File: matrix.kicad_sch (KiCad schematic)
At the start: 136 parts

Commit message: added some submodules
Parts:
- D1, D10, D11, D12, D13, D14, D15, D16, D17, D18, D19, D2, D20, D21, D22, D23, D24, D25, D26, D27, D28, D29, D3, D30, D31, D32, D33, D34, D35, D36, D37, D38, D39, D4, D40, D41, D42, D43, D44, D45, D46, D47, D48, D49, D5, D50, D51, D52, D53, D54, D55, D56, D57, D58, D59, D6, D60, D61, D62, D63, D64, D65, D66, D67, D68, D7, D8, D9: renamed from D?; footprint (none) -> Diode_SMD:D_SOD-123
- SW10: renamed from SW?; value MX_LED -> #8
- SW11: renamed from SW?; value MX_LED -> #9
- SW12: renamed from SW?; value MX_LED -> #0
- SW13: renamed from SW?; value MX_LED -> -_
- SW14: renamed from SW?; value MX_LED -> =+
- SW15: renamed from SW?; value MX_LED -> BKSP
- SW16: renamed from SW?; value MX_LED -> DEL
- SW17: renamed from SW?; value MX_LED -> TAB
- SW18: renamed from SW?; value MX_LED -> Q
- SW19: renamed from SW?; value MX_LED -> W
- SW2: renamed from SW?; value MX_LED -> Esc
- SW20: renamed from SW?; value MX_LED -> E
- SW21: renamed from SW?; value MX_LED -> R
- SW22: renamed from SW?; value MX_LED -> T
- SW23: renamed from SW?; value MX_LED -> Y
- SW24: renamed from SW?; value MX_LED -> U
- SW25: renamed from SW?; value MX_LED -> I
- SW26: renamed from SW?; value MX_LED -> O
- SW27: renamed from SW?; value MX_LED -> P
- SW28: renamed from SW?; value MX_LED -> [{
- SW29: renamed from SW?; value MX_LED -> ]}
- SW3: renamed from SW?; value MX_LED -> #1
- SW30: renamed from SW?; value MX_LED -> \|
- SW31: renamed from SW?; value MX_LED -> HOME
- SW32: renamed from SW?; value MX_LED -> CPLK
- SW33: renamed from SW?; value MX_LED -> A
- SW34: renamed from SW?; value MX_LED -> S
- SW35: renamed from SW?; value MX_LED -> D
- SW36: renamed from SW?; value MX_LED -> F
- SW37: renamed from SW?; value MX_LED -> G
- SW38: renamed from SW?; value MX_LED -> H
- SW39: renamed from SW?; value MX_LED -> J
- SW4: renamed from SW?; value MX_LED -> #2
- SW40: renamed from SW?; value MX_LED -> K
- SW41: renamed from SW?; value MX_LED -> L
- SW42: renamed from SW?; value MX_LED -> ;:
- SW43: renamed from SW?; value MX_LED -> '"
- SW44: renamed from SW?; value MX_LED -> ENTER
- SW45: renamed from SW?; value MX_LED -> PGUP
- SW46: renamed from SW?; value MX_LED -> LSHFT
- SW47: renamed from SW?; value MX_LED -> Z
- SW48: renamed from SW?; value MX_LED -> X
- SW49: renamed from SW?; value MX_LED -> C
- SW5: renamed from SW?; value MX_LED -> #3
- SW50: renamed from SW?; value MX_LED -> V
- SW51: renamed from SW?; value MX_LED -> B
- SW52: renamed from SW?; value MX_LED -> N
- SW53: renamed from SW?; value MX_LED -> M
- SW54: renamed from SW?; value MX_LED -> ,<
- SW55: renamed from SW?; value MX_LED -> .>
- SW56: renamed from SW?; value MX_LED -> /?
- SW57: renamed from SW?; value MX_LED -> RSHFT
- SW58: renamed from SW?; value MX_LED -> UP
- SW59: renamed from SW?; value MX_LED -> PGDN
- SW6: renamed from SW?; value MX_LED -> #4
- SW60: renamed from SW?; value MX_LED -> CTRL
- SW61: renamed from SW?; value MX_LED -> WIN
- SW62: renamed from SW?; value MX_LED -> LALT
- SW63: renamed from SW?; value MX_LED -> SPACE
- SW64: renamed from SW?; value MX_LED -> RALT
- SW65: renamed from SW?; value MX_LED -> FN
- SW66: renamed from SW?; value MX_LED -> FN2
- SW67: renamed from SW?; value MX_LED -> LEFT
- SW68: renamed from SW?; value MX_LED -> DOWN
- SW69: renamed from SW?; value MX_LED -> RIGHT
- SW7: renamed from SW?; value MX_LED -> #5
- SW8: renamed from SW?; value MX_LED -> #6
- SW9: renamed from SW?; value MX_LED -> #7

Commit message: half wiring done
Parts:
- D1: value D_Small -> ESC
- D10: value D_Small -> #9
- D11: value D_Small -> #0
- D12: value D_Small -> -_
- D13: value D_Small -> =+
- D14: value D_Small -> BKSP
- D15: value D_Small -> DEL
- D16: value D_Small -> TAB
- D17: value D_Small -> Q
- D18: value D_Small -> W
- D19: value D_Small -> E
- D2: value D_Small -> #1
- D20: value D_Small -> R
- D21: value D_Small -> T
- D22: value D_Small -> Y
- D23: value D_Small -> U
- D24: value D_Small -> I
- D25: value D_Small -> O
- D26: value D_Small -> P
- D27: value D_Small -> [{
- D28: value D_Small -> ]}
- D29: value D_Small -> \|
- D3: value D_Small -> #2
- D30: value D_Small -> HOME
- D31: value D_Small -> CPLK
- D32: value D_Small -> A
- D33: value D_Small -> S
- D34: value D_Small -> D
- D35: value D_Small -> F
- D36: value D_Small -> G
- D37: value D_Small -> H
- D38: value D_Small -> J
- D39: value D_Small -> K
- D4: value D_Small -> #3
- D40: value D_Small -> L
- D41: value D_Small -> ;:
- D42: value D_Small -> '"
- D43: value D_Small -> ENTER
- D44: value D_Small -> PGUP
- D45: value D_Small -> LSHFT
- D46: value D_Small -> Z
- D47: value D_Small -> X
- D48: value D_Small -> C
- D49: value D_Small -> V
- D5: value D_Small -> #4
- D50: value D_Small -> B
- D51: value D_Small -> N
- D52: value D_Small -> M
- D53: value D_Small -> ,<
- D54: value D_Small -> .>
- D55: value D_Small -> /?
- D56: value D_Small -> RSHFT
- D57: value D_Small -> UP
- D58: value D_Small -> PGDN
- D59: value D_Small -> CTRL
- D6: value D_Small -> #5
- D60: value D_Small -> WIN
- D61: value D_Small -> LALT
- D62: value D_Small -> SPACE
- D63: value D_Small -> RALT
- D64: value D_Small -> FN
- D65: value D_Small -> FN2
- D66: value D_Small -> LEFT
- D67: value D_Small -> DOWN
- D68: value D_Small -> RIGHT
- D7: value D_Small -> #6
- D8: value D_Small -> #7
- D9: value D_Small -> #8
- SW10, SW11, SW12, SW13, SW14, SW16, SW18, SW19, SW2, SW20, SW21, SW22, SW23, SW24, SW25, SW26, SW27, SW28, SW29, SW3, SW31, SW33, SW34, SW35, SW36, SW37, SW38, SW39, SW4, SW40, SW41, SW42, SW43, SW45, SW47, SW48, SW49, SW5, SW50, SW51, SW52, SW53, SW54, SW55, SW56, SW58, SW59, SW6, SW64, SW65, SW66, SW67, SW68, SW69, SW7, SW8, SW9: footprint (none) -> MX_Alps_Hybrid:MX-1U-NoLED
- SW15: footprint (none) -> MX_Alps_Hybrid:MX-2U-NoLED
- SW17, SW30, SW60: footprint (none) -> MX_Alps_Hybrid:MX-1.5U-NoLED
- SW32, SW57: footprint (none) -> MX_Alps_Hybrid:MX-1.75U-NoLED
- SW44, SW46: footprint (none) -> MX_Alps_Hybrid:MX-2.25U-NoLED
- SW61, SW62: footprint (none) -> MX_Alps_Hybrid:MX-1.25U-NoLED
- SW63: footprint (none) -> MX_Alps_Hybrid:MX-6U-NoLED

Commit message: Finished the design
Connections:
- net COL10 is gone; now on net COL5: SW12.2, SW27.2, SW42.2, SW55.2, SW65.2
- net COL11 is gone; now on net COL5: SW13.2, SW28.2, SW43.2, SW56.2, SW66.2
- net COL12 is gone; now on net COL6: SW14.2, SW29.2, SW57.2, SW67.2
- net COL13 is gone; now on net COL6: SW15.2, SW30.2, SW44.2, SW58.2, SW68.2
- net COL14 is gone; now on net COL7: SW16.2, SW31.2, SW45.2, SW59.2, SW69.2
- net COL8 is gone; now on net COL4: SW10.2, SW25.2, SW40.2, SW53.2
- net COL9 is gone; now on net COL4: SW11.2, SW26.2, SW41.2, SW54.2, SW64.2
- net COL0: now also SW18.2, SW3.2, SW33.2, SW61.2
- net COL1: now also SW19.2, SW20.2, SW34.2, SW35.2, SW4.2, SW47.2, SW48.2, SW5.2, SW62.2; no longer SW18.2, SW3.2, SW33.2, SW61.2
- net COL2: now also SW21.2, SW22.2, SW36.2, SW37.2, SW49.2, SW50.2, SW6.2, SW63.2, SW7.2; no longer SW19.2, SW34.2, SW4.2, SW47.2, SW62.2
- net COL3: now also SW23.2, SW24.2, SW38.2, SW39.2, SW51.2, SW52.2, SW8.2, SW9.2; no longer SW20.2, SW35.2, SW48.2, SW5.2
- net COL4: no longer SW21.2, SW36.2, SW49.2, SW6.2
- net COL5: no longer SW22.2, SW37.2, SW50.2, SW63.2, SW7.2
- net COL6: no longer SW23.2, SW38.2, SW51.2, SW8.2
- net COL7: no longer SW24.2, SW39.2, SW52.2, SW9.2

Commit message: Limpieza de routing y remplazo de footprints
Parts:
- D1, D10, D11, D12, D13, D14, D15, D16, D17, D18, D19, D2, D20, D21, D22, D23, D24, D25, D26, D27, D28, D29, D3, D30, D31, D32, D33, D34, D35, D36, D37, D38, D39, D4, D40, D41, D42, D43, D44, D45, D46, D47, D48, D49, D5, D50, D51, D52, D53, D54, D55, D56, D57, D58, D59, D6, D60, D61, D62, D63, D64, D65, D66, D67, D68, D7, D8, D9: footprint Diode_SMD:D_SOD-123 -> cftkb:D_DO-35_SOD27_P5.08mm_Horizontal
- SW10, SW11, SW12, SW13, SW14, SW16, SW18, SW19, SW2, SW20, SW21, SW22, SW23, SW24, SW25, SW26, SW27, SW28, SW29, SW3, SW31, SW33, SW34, SW35, SW36, SW37, SW38, SW39, SW4, SW40, SW41, SW42, SW43, SW45, SW47, SW48, SW49, SW5, SW50, SW51, SW52, SW53, SW54, SW55, SW56, SW58, SW59, SW6, SW64, SW65, SW66, SW67, SW68, SW69, SW7, SW8, SW9: footprint MX_Alps_Hybrid:MX-1U-NoLED -> MX_Only:MXOnly-1U-Hotswap
- SW15: footprint MX_Alps_Hybrid:MX-2U-NoLED -> MX_Only:MXOnly-2U-Hotswap
- SW17, SW30, SW60: footprint MX_Alps_Hybrid:MX-1.5U-NoLED -> MX_Only:MXOnly-1.5U-Hotswap
- SW32, SW57: footprint MX_Alps_Hybrid:MX-1.75U-NoLED -> MX_Only:MXOnly-1.75U-Hotswap
- SW44, SW46: footprint MX_Alps_Hybrid:MX-2.25U-NoLED -> MX_Only:MXOnly-2.25U-Hotswap
- SW61, SW62: footprint MX_Alps_Hybrid:MX-1.25U-NoLED -> MX_Only:MXOnly-1.25U-Hotswap
- SW63: footprint MX_Alps_Hybrid:MX-6U-NoLED -> MX_Only:MXOnly-6U-Centered-Hotswap

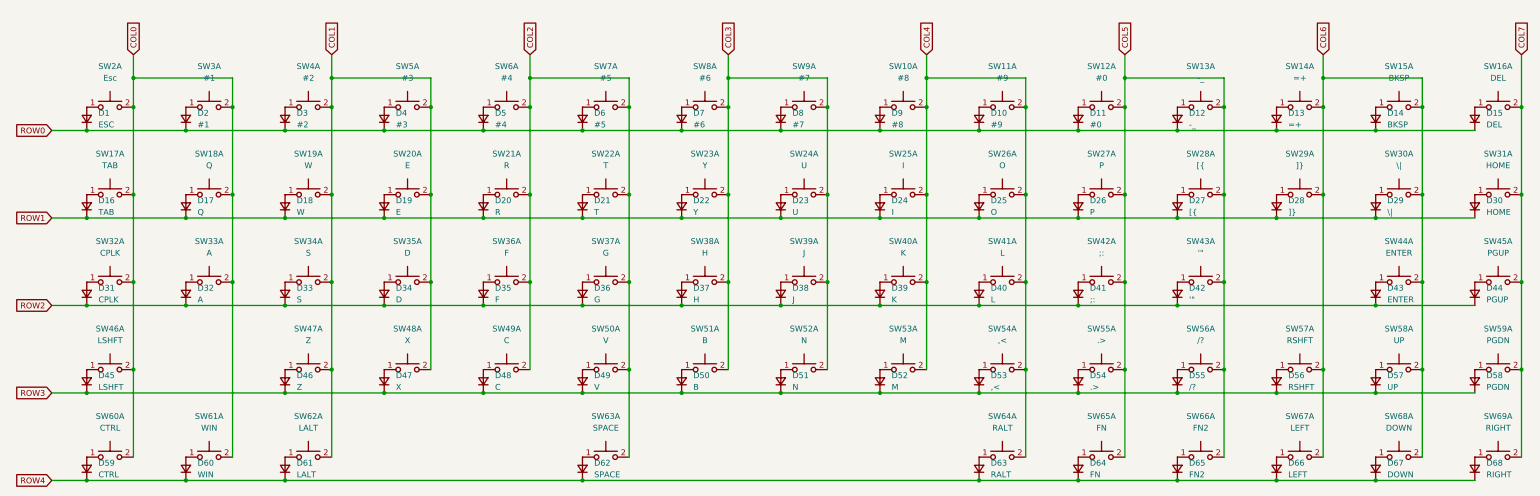
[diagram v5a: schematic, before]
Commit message: Added rgb underglow
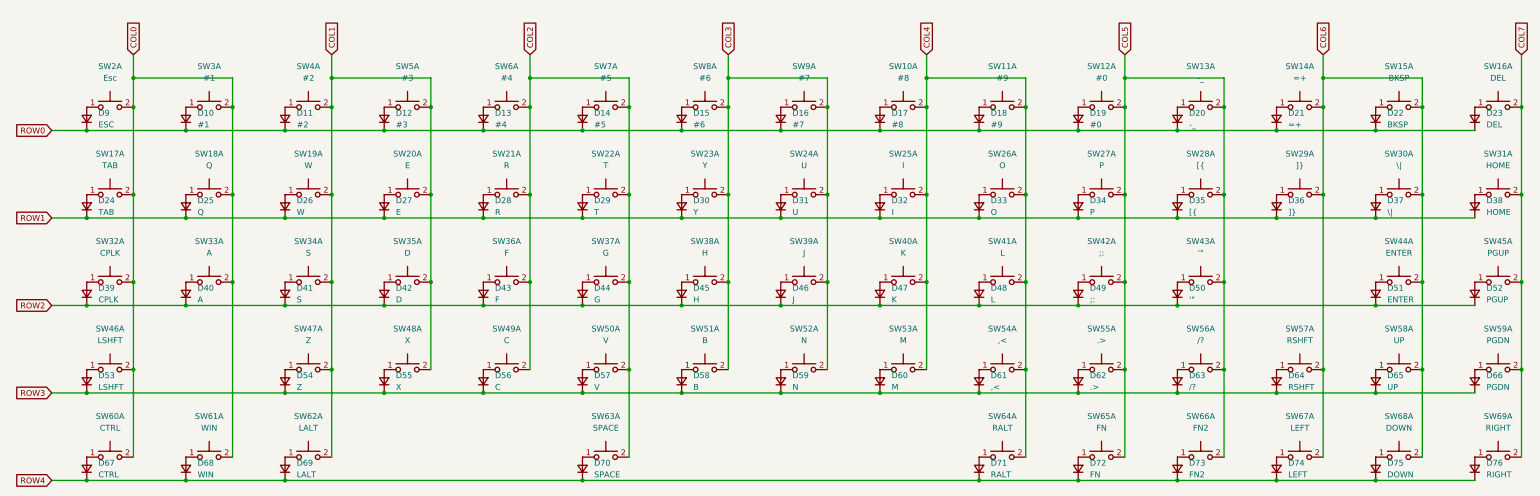
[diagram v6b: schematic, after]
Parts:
- renumbered D2 to D10, D3 to D11, D4 to D12, D5 to D13, D6 to D14, D7 to D15, D8 to D16, D9 to D17, D10 to D18, D11 to D19, D12 to D20, D13 to D21, D14 to D22, D15 to D23, D16 to D24, D17 to D25, D18 to D26, D19 to D27, D20 to D28, D21 to D29, D22 to D30, D23 to D31, D24 to D32, D25 to D33, D26 to D34, D27 to D35, D28 to D36, D29 to D37, D30 to D38, D31 to D39, D32 to D40, D33 to D41, D34 to D42, D35 to D43, D36 to D44, D37 to D45, D38 to D46, D39 to D47, D40 to D48, D41 to D49, D42 to D50, D43 to D51, D44 to D52, D45 to D53, D46 to D54, D47 to D55, D48 to D56, D49 to D57, D50 to D58, D51 to D59, D52 to D60, D53 to D61, D54 to D62, D55 to D63, D56 to D64, D57 to D65, D58 to D66, D59 to D67, D60 to D68, D61 to D69, D62 to D70, D63 to D71, D64 to D72, D65 to D73, D66 to D74, D67 to D75, D68 to D76, D1 to D9
